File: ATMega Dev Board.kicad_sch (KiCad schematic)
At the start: 55 parts, among them J1 Conn_01x13, J2 Conn_01x09, J3 SPI header, J4 USB-C_31-M-12, Q1 S8050, Q2 2N7002, Q3 HL6042, Q4 HL6042, SW1 SW_SPST, SW2 SW_SPST, U1 ATmega32A-A, U2 CH340X, U3 USBLC6-2P6, X1 16MHz

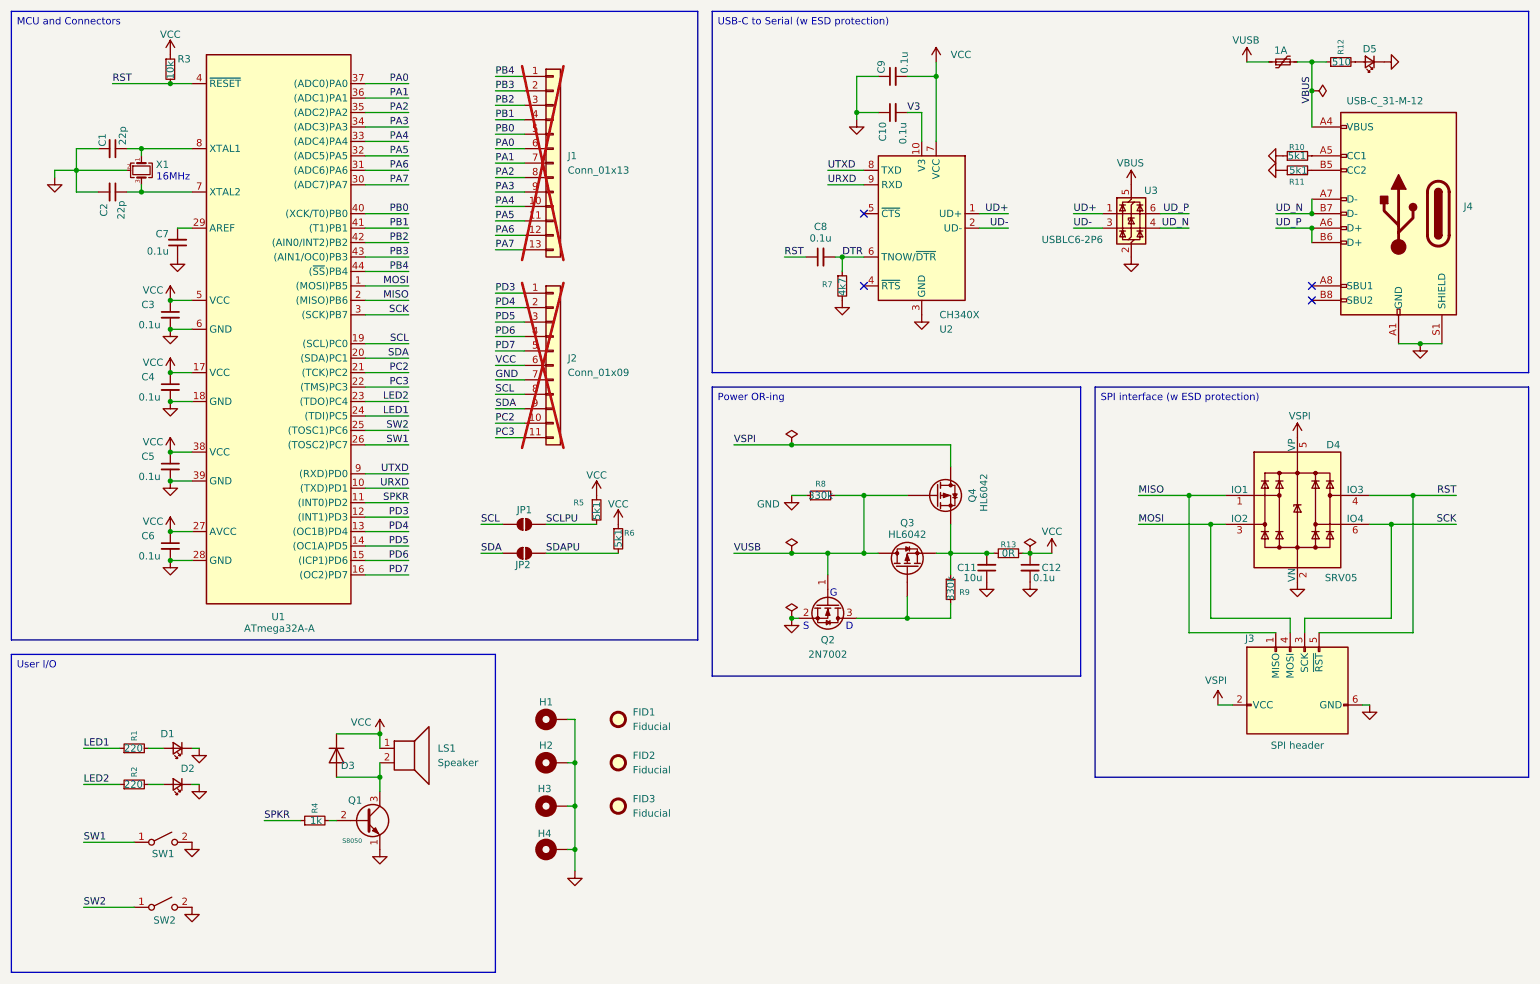
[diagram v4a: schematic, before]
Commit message: added ADC/AREF components
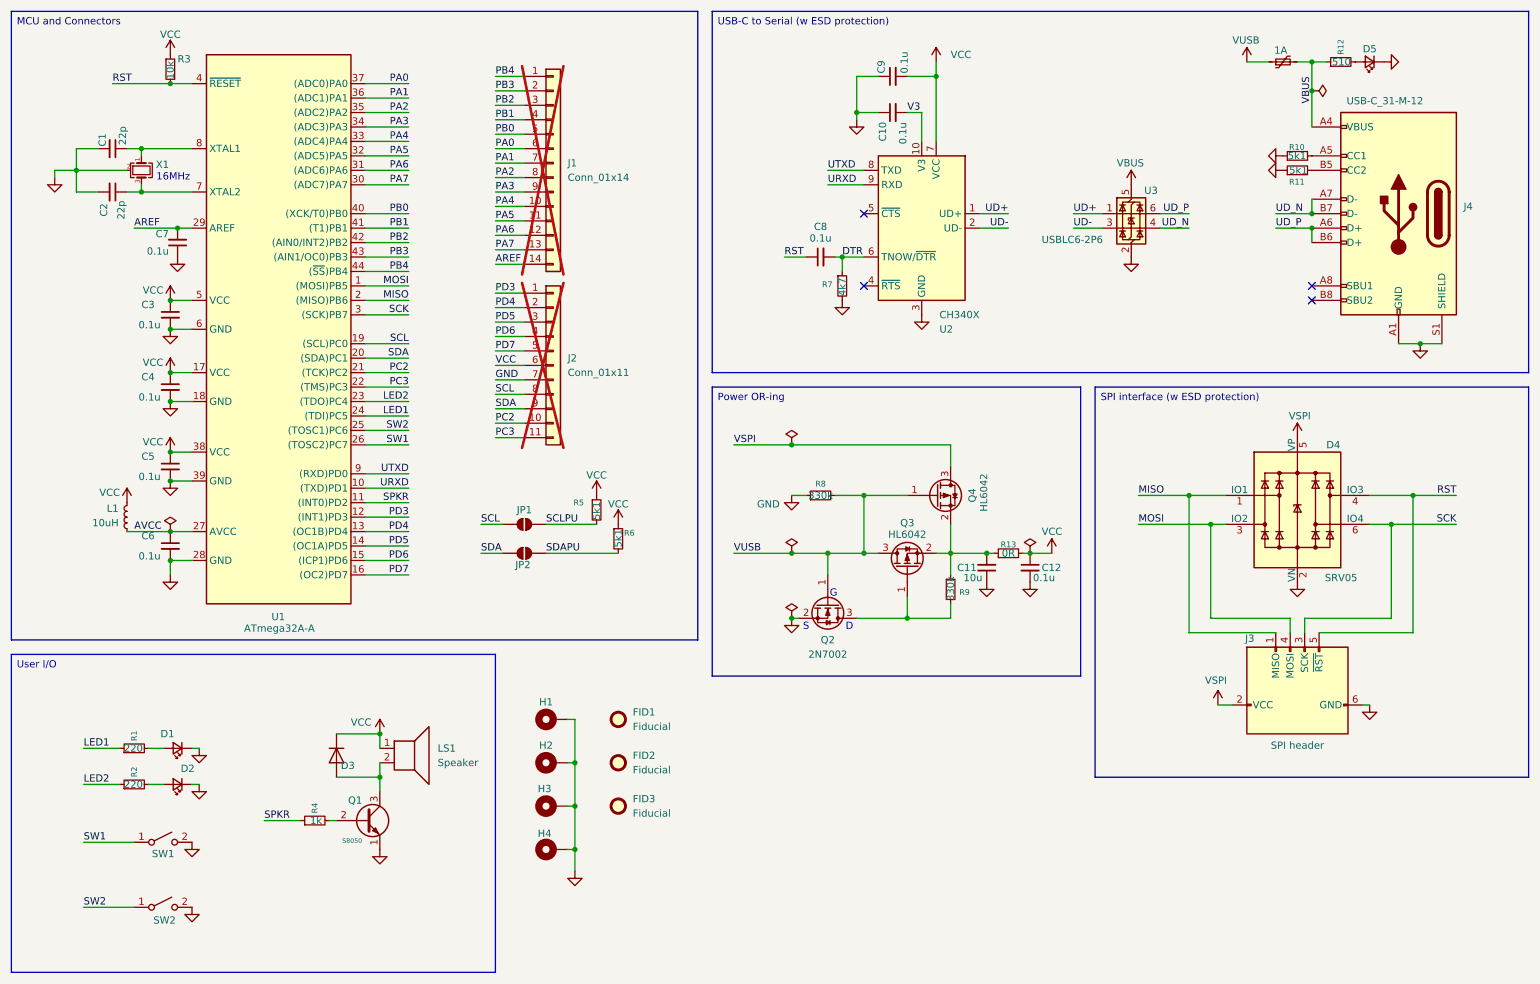
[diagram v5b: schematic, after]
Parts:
- added L1: 10uH, Inductor_SMD:L_0805_2012Metric, symbol Device:L_Small
- J1: value Conn_01x13 -> Conn_01x14; footprint Connector_PinSocket_2.54mm:PinSocket_1x13_P2.54mm_Vertical -> Connector_PinSocket_2.54mm:PinSocket_1x14_P2.54mm_Vertical; symbol Connector_Generic:Conn_01x13 -> Connector_Generic:Conn_01x14; LCSC C2897372 -> C2905420; now in the parts list
- J2: value Conn_01x09 -> Conn_01x11; LCSC C2897372 -> C25503117
- Q3, Q4: symbol Device:Q_PMOS -> Transistor_FET:Q_PMOS_GSD
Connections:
- net VCC: now also L1.1; no longer C6.1, U1.27 (AVCC)
- net VSPI: now also Q4.3 (D); no longer Q4.D
- net VUSB: now also Q3.3 (D), Q4.1 (G); no longer Q3.D, Q4.G
- net at C11.2, R13.1, R9.1: now also Q3.2 (S), Q4.2 (S); no longer Q3.S, Q4.S
- net at Q2.3 (D), R9.2: now also Q3.1 (G); no longer Q3.G
- net AREF: now reaches C7.2, U1.29 (AREF)
- net AREF: now also J1.14 (Pin_14)
- new net AVCC: C6.1, L1.2, U1.27 (AVCC)

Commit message: changed part#t
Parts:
- R11: LCSC C21189 -> C23186
- R13: LCSC (none) -> C21189
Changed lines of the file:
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@@
 			)
 		)
-		(property "LCSC" "C21189"
+		(property "LCSC" "C23186"
 			(at 241.3 43.18 0)
 			(effects
@@
 			(effects
 				(font
+					(size 1.27 1.27)
+				)
+				(hide yes)
+			)
+		)
+		(property "LCSC" "C21189"
+			(at 190.5 108.966 0)
+			(effects
+				(font

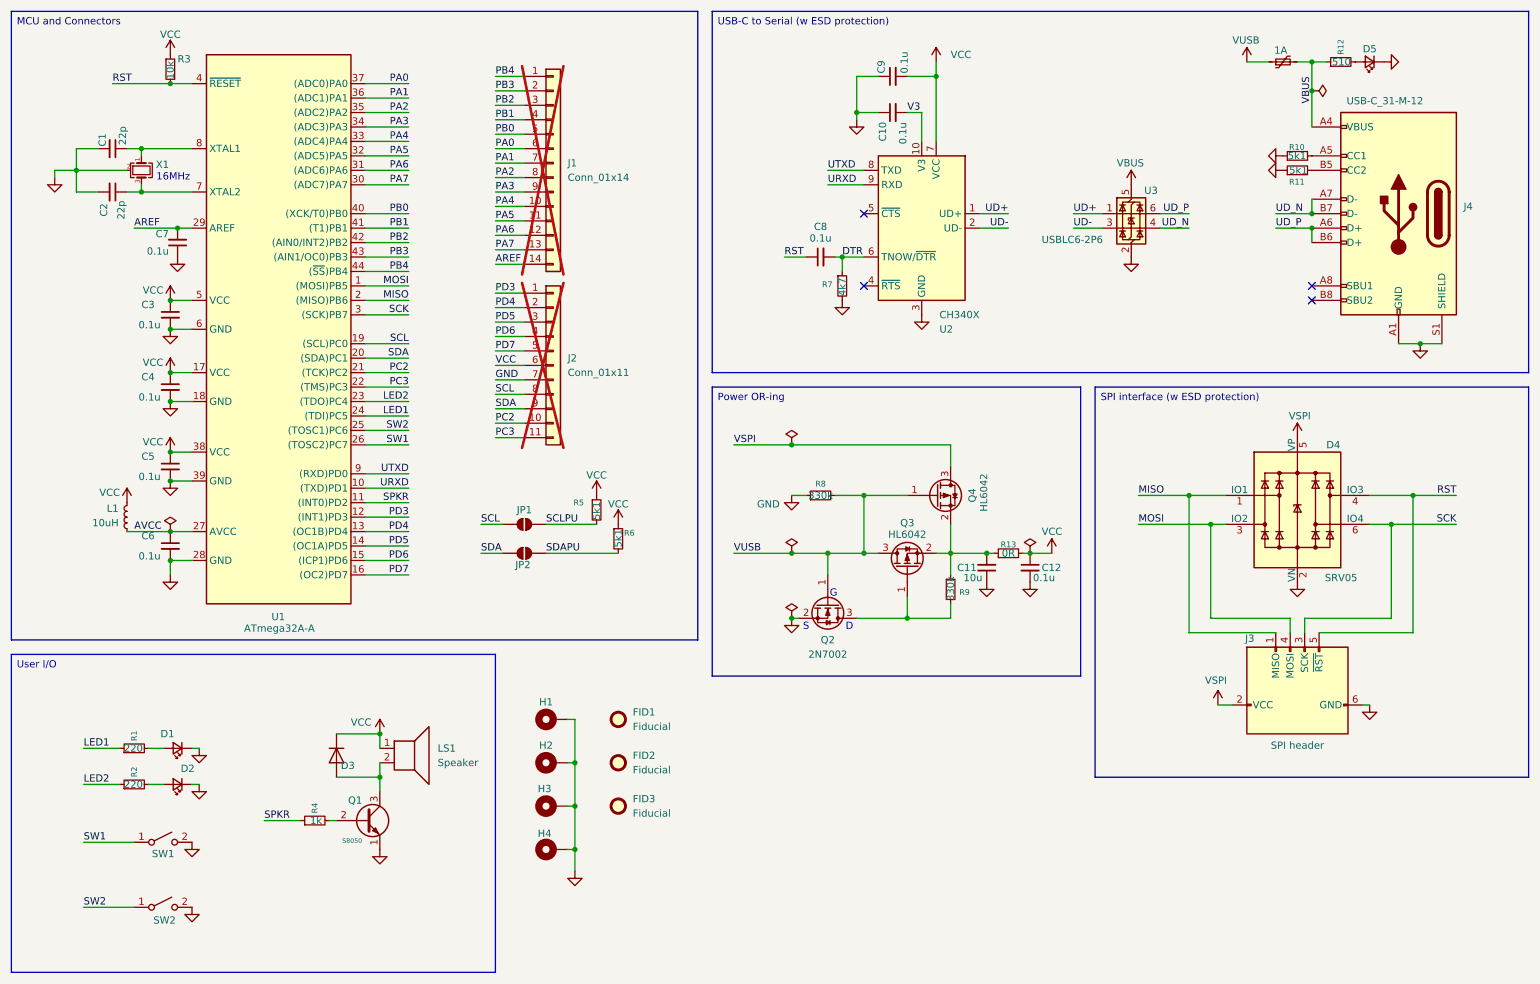
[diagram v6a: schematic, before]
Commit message: added VBUS capacitor
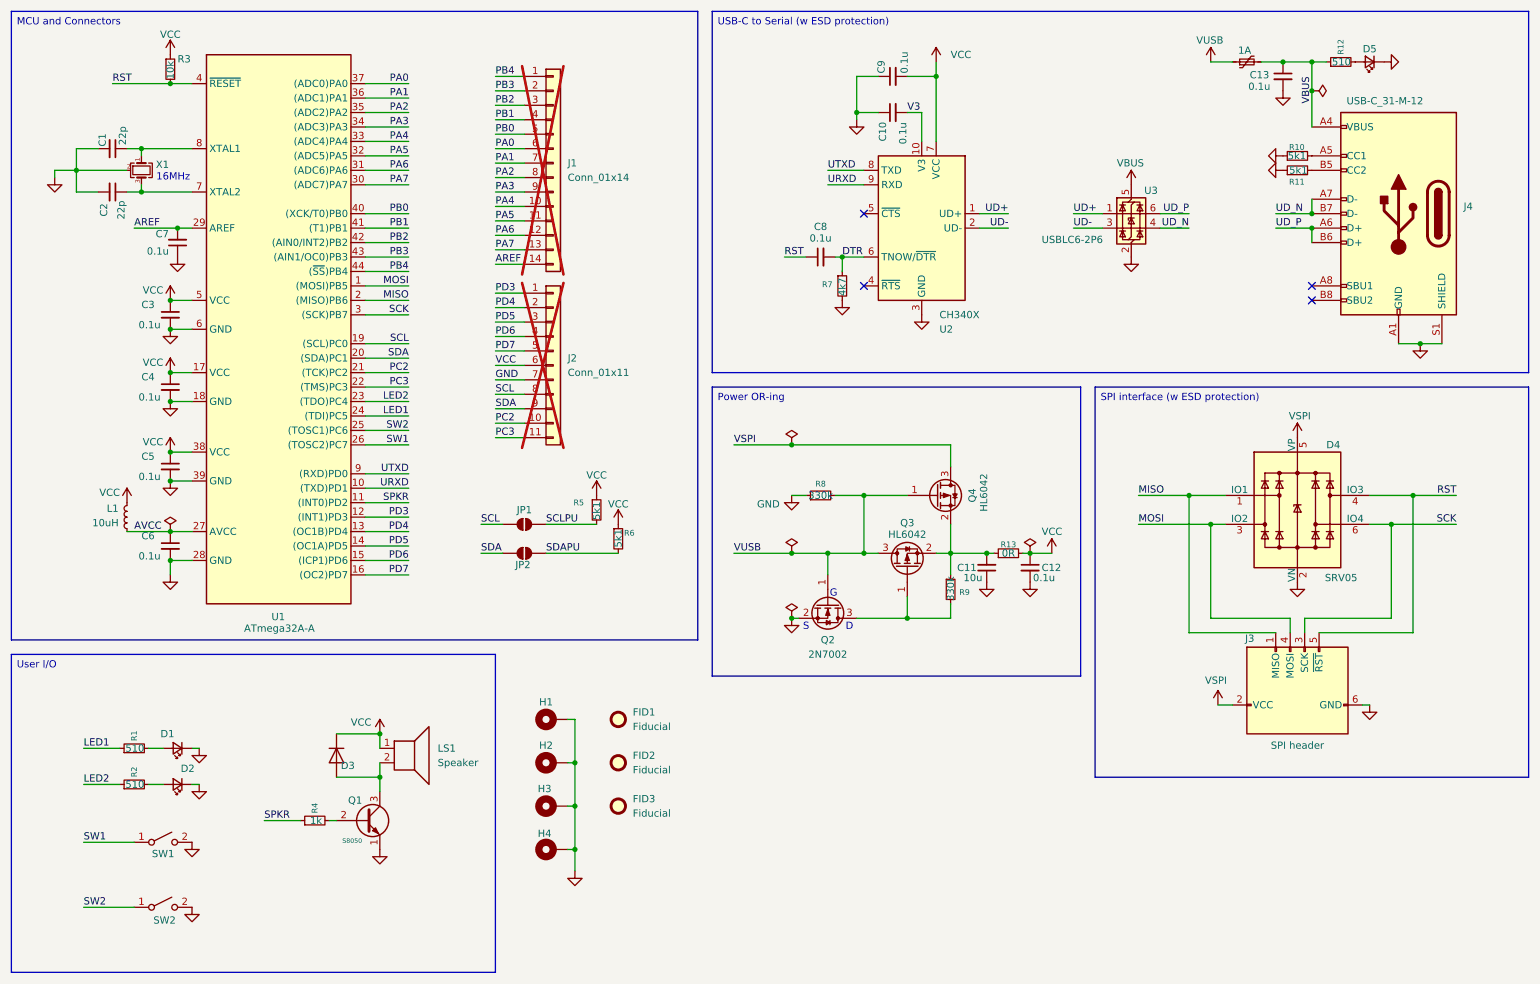
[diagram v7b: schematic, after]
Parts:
- added C13: 0.1u, Capacitor_SMD:C_0603_1608Metric, symbol Device:C_Small
- R1, R2: value 220 -> 510; LCSC C22962 -> C23193
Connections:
- net GND: now also C13.2
- net VBUS: now also C13.1

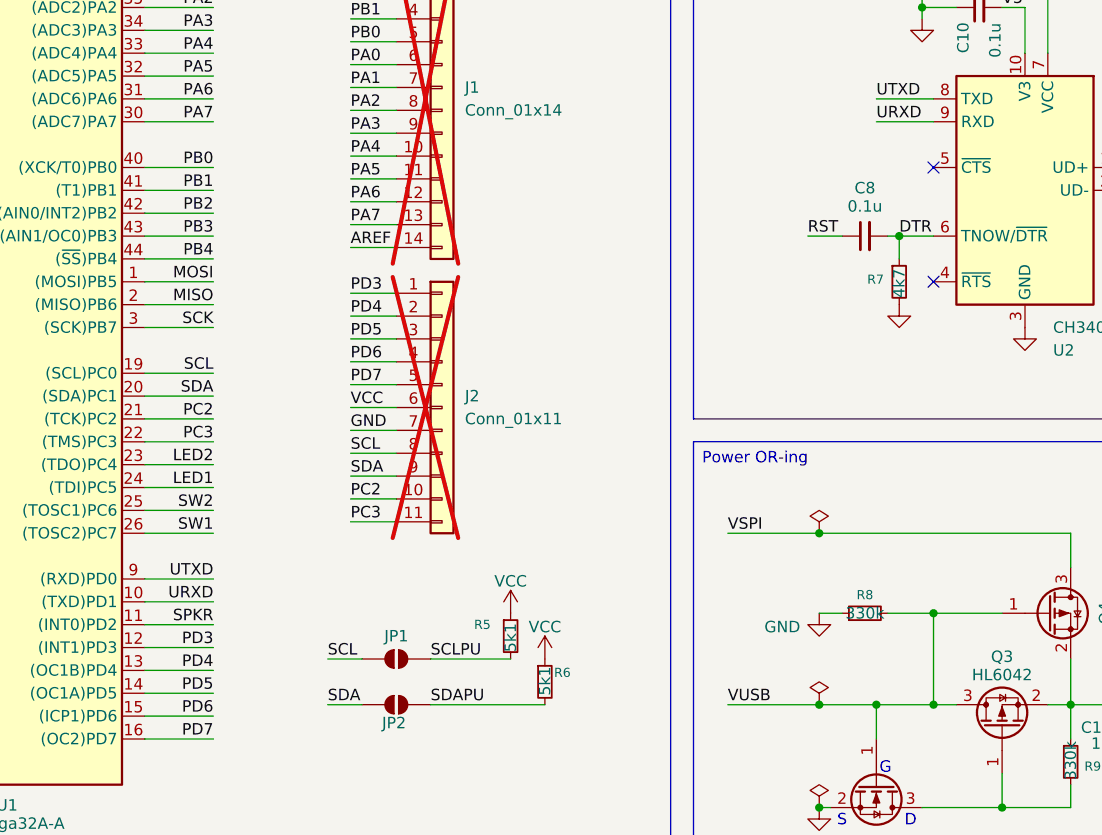
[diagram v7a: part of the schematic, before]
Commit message: fixed CH340X DTR setup
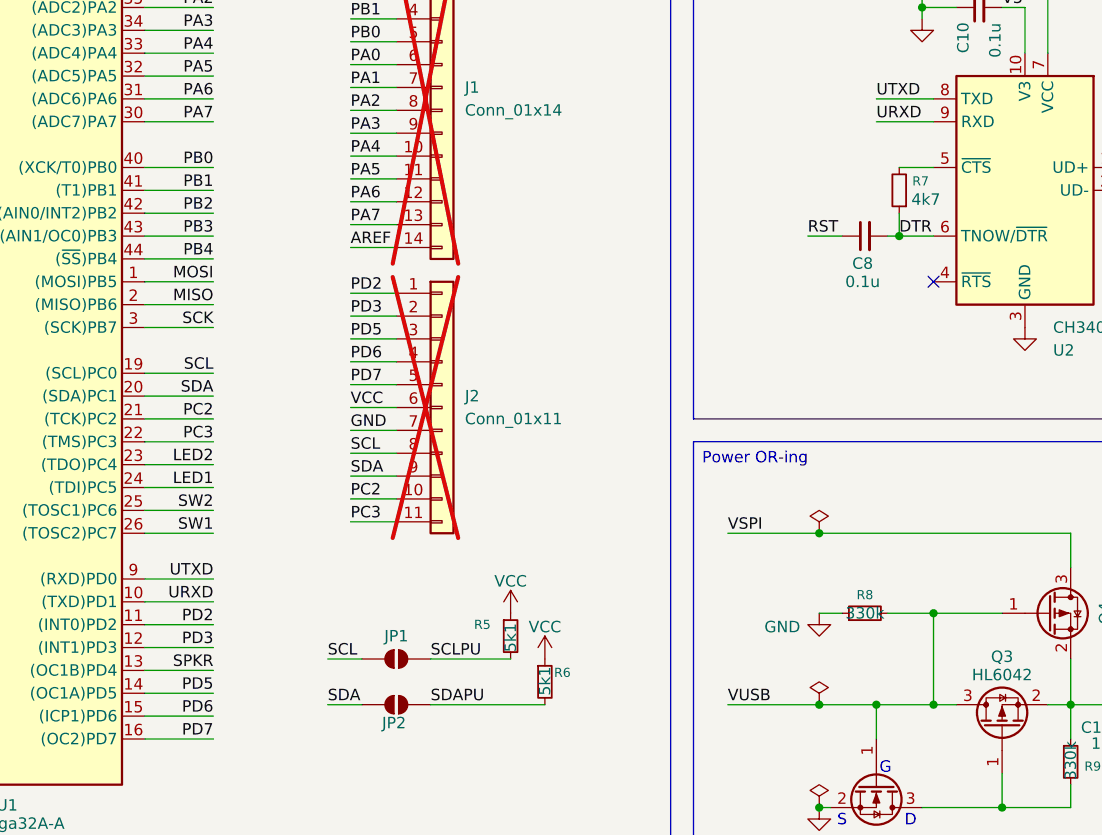
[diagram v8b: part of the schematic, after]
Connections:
- net GND: no longer R7.2
- net PD3: now also J2.2 (Pin_2); no longer J2.1 (Pin_1)
- net SPKR: now also U1.13 ((OC1B)PD4); no longer U1.11 ((INT0)PD2)
- net at U2.5 (~{CTS}): now also R7.2
- removed net PD4: J2.2 (Pin_2), U1.13 ((OC1B)PD4)
- new net PD2: J2.1 (Pin_1), U1.11 ((INT0)PD2)
- no-connect marks 4 -> 3
